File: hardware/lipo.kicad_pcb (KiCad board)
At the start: 2 copper layers, 70 x 50 mm, 59 parts

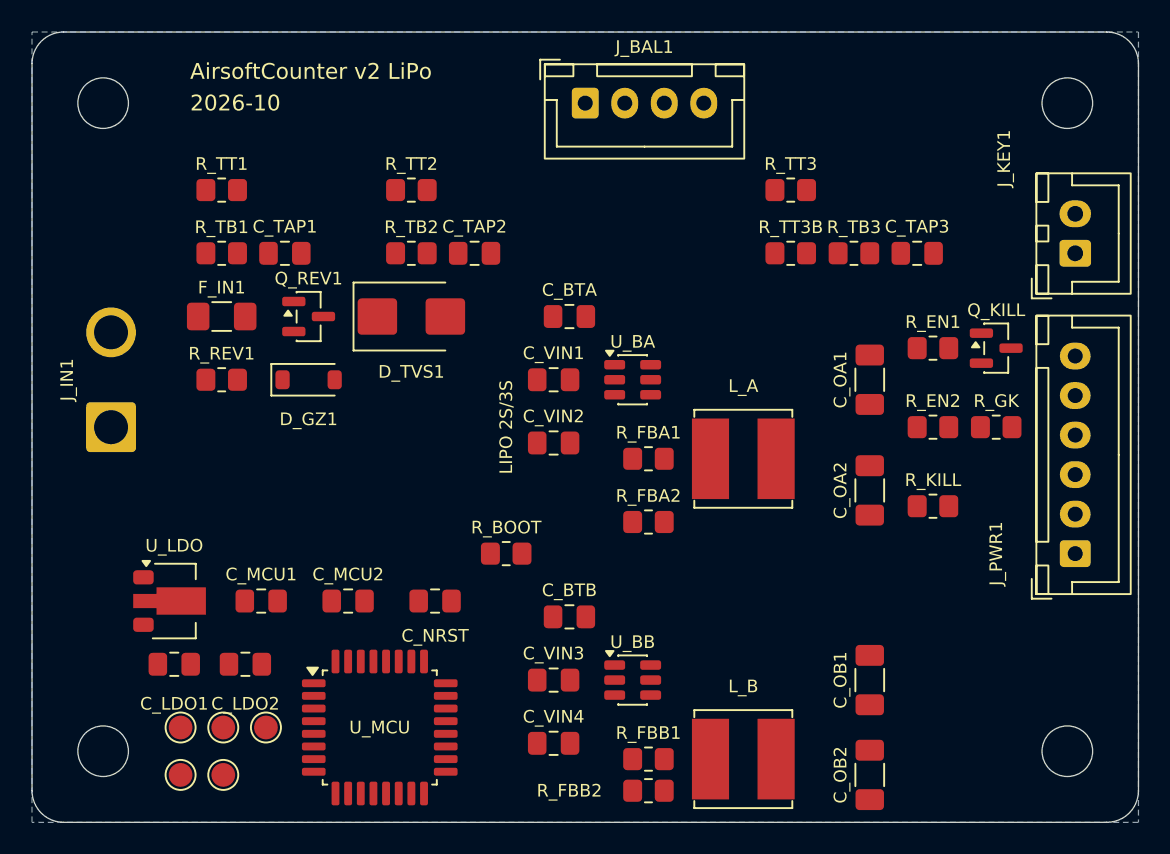
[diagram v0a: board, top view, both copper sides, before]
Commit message: hardware: LiPo board routed, fab package
Freerouting: 462 tracks/vias, 0 unrouted. ERC 0, DRC 0 violations, 0 schematic
parity issues. The two SW nodes moved from the Power class to Default: the
stock TSOT-23-6 SW pad (0.95 mm pitch) cannot take a 0.8 mm track, so
Freerouting left it unrouted. fab/lipo/: gerbers 11 files, outline 70x50,
PTH 0.3/0.95/1.0/2.15 mm, 4 x 3.2 mm NPTH; the JLC BOM/CPL leave out J_IN1 and
the five test pads. make boards rebuilds the carrier and both pack boards
unchanged.

Co-Authored-By: Claude Opus 5.5 <noreply@anthropic.com>
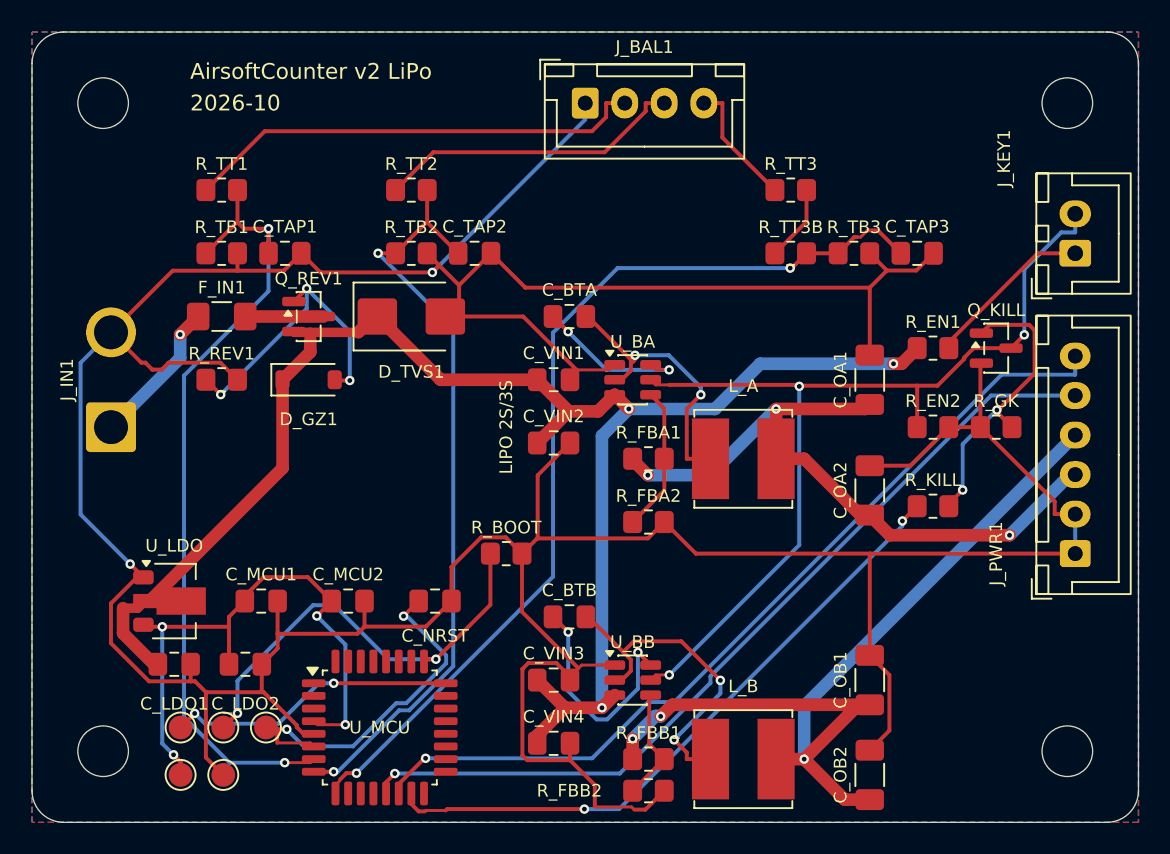
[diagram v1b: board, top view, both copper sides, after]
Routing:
- net GND: track 0.00 -> 292.5 mm, vias 0 -> 2
- net VIN: track 0.00 -> 103.8 mm, vias 0 -> 3
- net TAP3_ADC: track 0.00 -> 60.5 mm, vias 0 -> 2
- net BUCK_EN: track 0.00 -> 60.3 mm, vias 0 -> 3
- net +5V: track 0.00 -> 57.0 mm, vias 0 -> 3
- net SCL_EXT: track 0.00 -> 55.3 mm, vias 0 -> 1
- net SDA_EXT: track 0.00 -> 54.7 mm, vias 0 -> 1
- net TAP1_ADC: track 0.00 -> 51.1 mm, vias 0 -> 2
- net TAP2_ADC: track 0.00 -> 48.4 mm, vias 0 -> 2
- net VBAT_SW: track 0.00 -> 43.0 mm, vias 0 -> 3
- net KILL_DRV: track 0.00 -> 41.0 mm, vias 0 -> 2
- net +3V3: track 0.00 -> 37.7 mm, vias 0 -> 4
- net BAL1: track 0.00 -> 29.3 mm
- net BOOT0: track 0.00 -> 28.2 mm, vias 0 -> 2
- net NRST: track 0.00 -> 22.9 mm, vias 0 -> 2
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- added copper zone on F.Cu, net GND

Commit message: hardware: LiPo board Extended types 7 -> 4
AO3407A -> AO3401A (Basic) with a 10 V MMSZ5240B (Preferred) gate clamp
under its 12 V VGS limit; SMBJ15A moves to the Preferred C19077569.
Checked against the live JLCPCB Basic/Preferred catalog.

Co-Authored-By: Claude Opus 5.5 <noreply@anthropic.com>
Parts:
- D_GZ1: value BZT52C12 -> MMSZ5240B
- Q_REV1: value AO3407A -> AO3401A
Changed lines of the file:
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@@
 			)
 		)
-		(property "Value" "BZT52C12"
+		(property "Value" "MMSZ5240B"
 			(at 0 2.1 0)
 			(layer "F.Fab")
@@
 			)
 		)
-		(property "Value" "AO3407A"
+		(property "Value" "AO3401A"
 			(at 0 2.4 0)
 			(layer "F.Fab")
